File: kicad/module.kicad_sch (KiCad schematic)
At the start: 11 parts, among them J2 Conn_01x12, J3 Conn_01x10, J4 Conn_01x02, Q1 SI2302CDS, SW1 CNK_KMR2, U8 RioteeModule

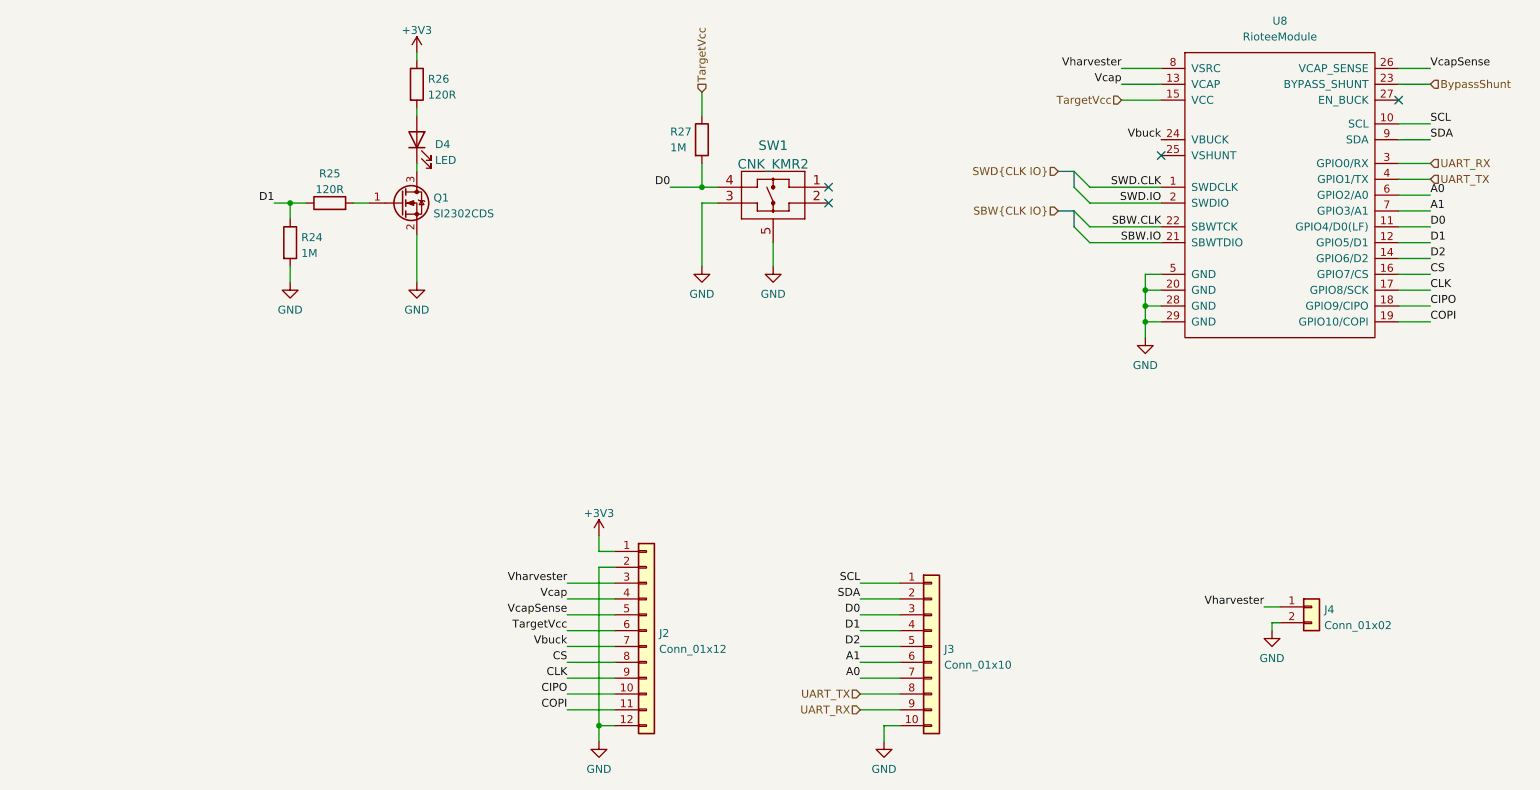
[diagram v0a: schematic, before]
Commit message: add fourth level converter for simultaneous programming + TX/RX
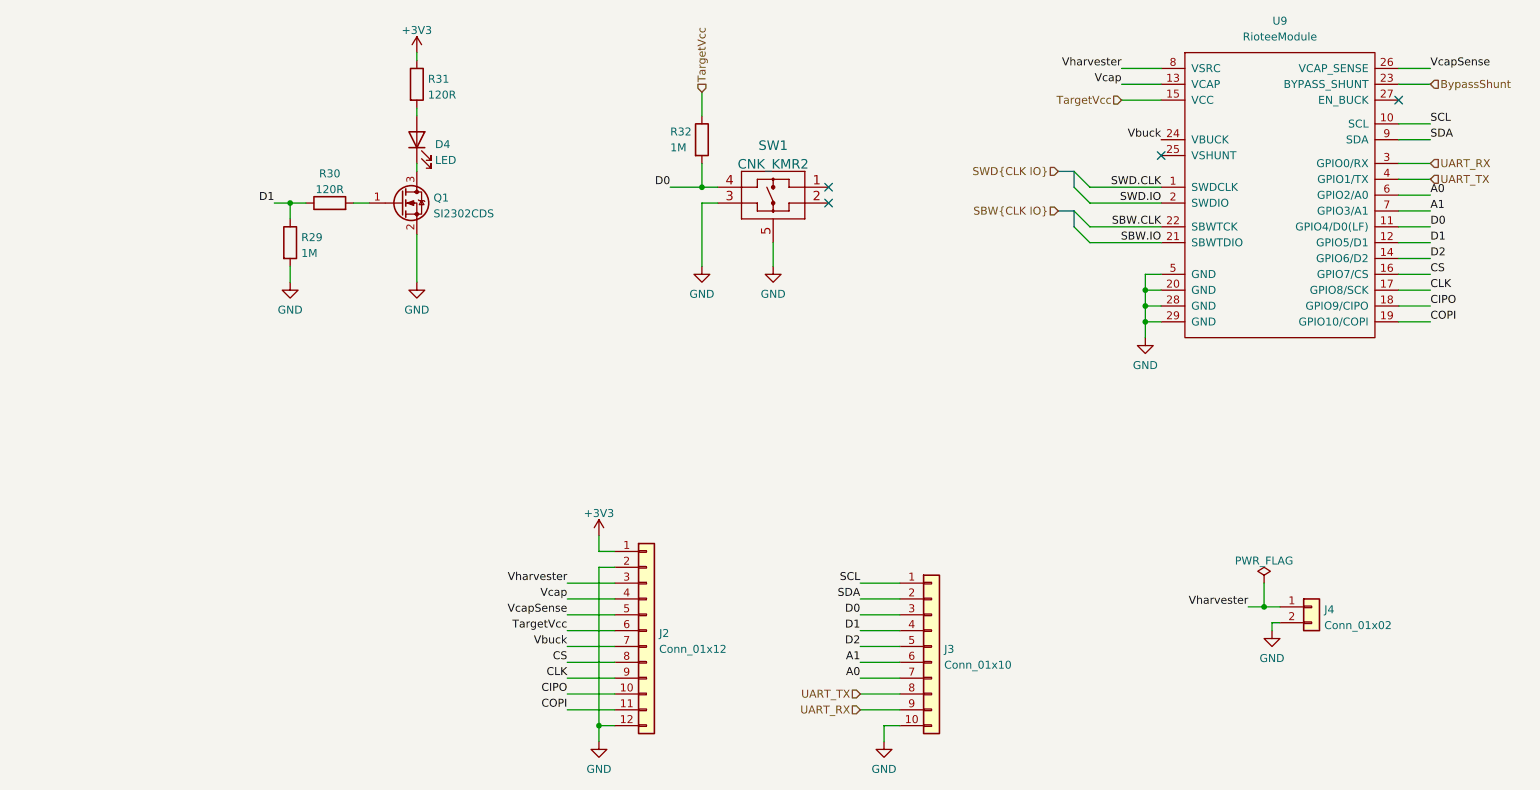
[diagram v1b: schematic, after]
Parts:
- renumbered R24 to R29, R25 to R30, R26 to R31, R27 to R32, U8 to U9

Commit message: replace target supply diode with analog switch
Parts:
- added C28: 0.1u, Capacitor_SMD:C_0402_1005Metric, symbol Device:C
- added R28: 5.1k, Resistor_SMD:R_0402_1005Metric, symbol Device:R
- added U9: TS5A3166YZP, riotee:TI_YZP0005, symbol riotee:TS5A3166YZP
- D3: renamed from D4; MPN (none) -> QBLP595-AG1
- J2: MPN (none) -> PPPC121LFBN-RC
- J3: MPN (none) -> PPPC101LFBN-RC
- J4: MPN (none) -> 620102131822
- Q1: MPN (none) -> SI2302CDS-T1-GE3
- R29, R32: MPN (none) -> WR04X1004FTL
- R30, R31: MPN (none) -> CR0402-FX-1200GLF
- SW1: MPN (none) -> KMR221NG LFS
- renumbered U9 to U10
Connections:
- net +3V3: now also C28.1, U9.A2 (V+)
- net GND: now also C28.2, R28.1, U9.C1 (GND)
- net TargetVcc: now also U9.A1
- new net +2V1: U9.B1
- new net TargetPowerEnable: R28.2, U9.C2

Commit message: rename pins and add component description
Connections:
- net GND: no longer SW1.5
- net CIPO renamed D9
- net CLK renamed D8
- net COPI renamed D10
- net CS renamed D7
- net D0 renamed D6
- net D1 renamed D5
- net D2 renamed D4
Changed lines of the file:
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@@
-    (stroke (width 0) (type default) (color 0 0 0 0))
-  )
-  (wire (pts (xy 135.89 60.96) (xy 135.89 64.77))
     (stroke (width 0) (type default) (color 0 0 0 0))
   )
@@
     (stroke (width 0) (type default) (color 0 0 0 0))
   )
-  (label "D1" (at 55.88 54.61 180)
+  (label "D5" (at 55.88 54.61 180)
     (effects (font (size 1.27 1.27)) (justify right bottom))
   )
@@
     (effects (font (size 1.27 1.27)) (justify right bottom))
   )
-  (label "COPI" (at 241.3 73.66 0)
+  (label "D10" (at 241.3 73.66 0)
     (effects (font (size 1.27 1.27)) (justify left bottom))
   )
@@
     (effects (font (size 1.27 1.27)) (justify right bottom))
   )
-  (label "D0" (at 119.38 52.07 180)
+  (label "D6" (at 119.38 52.07 180)
     (effects (font (size 1.27 1.27)) (justify right bottom))
   )
@@
     (effects (font (size 1.27 1.27)) (justify left bottom))
   )
-  (label "CS" (at 241.3 66.04 0)
+  (label "D7" (at 241.3 66.04 0)
     (effects (font (size 1.27 1.27)) (justify left bottom))
   )
@@
     (effects (font (size 1.27 1.27)) (justify right bottom))
   )
-  (label "COPI" (at 102.87 135.89 180)
+  (label "D10" (at 102.87 135.89 180)
     (effects (font (size 1.27 1.27)) (justify right bottom))
   )
@@
     (effects (font (size 1.27 1.27)) (justify right bottom))
   )
-  (label "CIPO" (at 102.87 133.35 180)
-    (effects (font (size 1.27 1.27)) (justify right bottom))
-  )
-  (label "D0" (at 149.86 120.65 180)
+  (label "D9" (at 102.87 133.35 180)
+    (effects (font (size 1.27 1.27)) (justify right bottom))
+  )
+  (label "D6" (at 149.86 120.65 180)
     (effects (font (size 1.27 1.27)) (justify right bottom))
   )
@@
     (effects (font (size 1.27 1.27)) (justify left bottom))
   )
-  (label "D2" (at 241.3 63.5 0)
-    (effects (font (size 1.27 1.27)) (justify left bottom))
-  )
-  (label "D0" (at 241.3 58.42 0)
+  (label "D4" (at 241.3 63.5 0)
+    (effects (font (size 1.27 1.27)) (justify left bottom))
+  )
+  (label "D6" (at 241.3 58.42 0)
     (effects (font (size 1.27 1.27)) (justify left bottom))
   )
@@
     (effects (font (size 1.27 1.27)) (justify right bottom))
   )
-  (label "D1" (at 241.3 60.96 0)
-    (effects (font (size 1.27 1.27)) (justify left bottom))
-  )
-  (label "D1" (at 149.86 123.19 180)
+  (label "D5" (at 241.3 60.96 0)
+    (effects (font (size 1.27 1.27)) (justify left bottom))
+  )
+  (label "D5" (at 149.86 123.19 180)
     (effects (font (size 1.27 1.27)) (justify right bottom))
   )
@@
     (effects (font (size 1.27 1.27)) (justify left bottom))
   )
-  (label "CIPO" (at 241.3 71.12 0)
+  (label "D9" (at 241.3 71.12 0)
     (effects (font (size 1.27 1.27)) (justify left bottom))
   )
@@
     (effects (font (size 1.27 1.27)) (justify right bottom))
   )
-  (label "CLK" (at 102.87 130.81 180)
-    (effects (font (size 1.27 1.27)) (justify right bottom))
-  )
-  (label "CLK" (at 241.3 68.58 0)
+  (label "D8" (at 102.87 130.81 180)
+    (effects (font (size 1.27 1.27)) (justify right bottom))
+  )
+  (label "D8" (at 241.3 68.58 0)
     (effects (font (size 1.27 1.27)) (justify left bottom))
   )
@@
     (effects (font (size 1.27 1.27)) (justify right bottom))
   )
-  (label "CS" (at 102.87 128.27 180)
-    (effects (font (size 1.27 1.27)) (justify right bottom))
-  )
-  (label "D2" (at 149.86 125.73 180)
+  (label "D7" (at 102.87 128.27 180)
+    (effects (font (size 1.27 1.27)) (justify right bottom))
+  )
+  (label "D4" (at 149.86 125.73 180)
     (effects (font (size 1.27 1.27)) (justify right bottom))
   )
@@
     )
     (property "MPN" "CR0402-FX-1200GLF" (id 4) (at 78.74 35.56 0)
+      (effects (font (size 1.27 1.27)) hide)
+    )
+    (property "Description" "Res, 0402, 1%" (id 5) (at 78.74 35.56 0)
       (effects (font (size 1.27 1.27)) hide)
     )
@@
       (effects (font (size 1.27 1.27)) hide)
     )
+    (property "Description" "Res, 0402, 1%" (id 5) (at 124.46 44.45 0)
+      (effects (font (size 1.27 1.27)) hide)
+    )
     (pin "1")
     (pin "2")
@@
       (effects (font (size 1.27 1.27)) hide)
     )
+    (property "Description" "Res, 0402, 1%" (id 5) (at 44.45 127 0)
+      (effects (font (size 1.27 1.27)) hide)
+    )
     (pin "1")
     (pin "2")
@@
     )
     (property "MPN" "CL05A104KA5NNNC" (id 4) (at 67.31 102.87 0)
+      (effects (font (size 1.27 1.27)) hide)
+    )
+    (property "Description" "Cap, 0402, X5R, 10V" (id 5) (at 67.31 102.87 0)
       (effects (font (size 1.27 1.27)) hide)
     )
@@
       (effects (font (size 1.27 1.27)) hide)
     )
+    (property "Description" "1-Ohm SPST switch" (id 5) (at 55.88 118.11 0)
+      (effects (font (size 1.27 1.27)) hide)
+    )
     (pin "A1")
     (pin "A2")
@@
       (effects (font (size 1.27 1.27)) hide)
     )
+    (property "Description" "Tactile SPST" (id 5) (at 135.89 53.34 0)
+      (effects (font (size 1.27 1.27)) hide)
+    )
     (pin "1")
     (pin "2")
     (pin "3")
     (pin "4")
-    (pin "5")
   )
   (symbol (lib_id "riotee:+2V1") (at 44.45 107.95 0) (unit 1)
@@
     )
     (property "MPN" "QBLP595-AG1" (id 4) (at 78.74 44.45 0)
+      (effects (font (size 1.27 1.27)) hide)
+    )
+    (property "Description" "LED, 0402, green, clear" (id 5) (at 78.74 44.45 0)
       (effects (font (size 1.27 1.27)) hide)
     )
@@
     )
     (property "MPN" "WR04X1004FTL" (id 4) (at 58.42 60.96 0)
+      (effects (font (size 1.27 1.27)) hide)
+    )
+    (property "Description" "Res, 0402, 1%" (id 5) (at 58.42 60.96 0)
       (effects (font (size 1.27 1.27)) hide)
     )
@@
     (pin "9")
   )
-  (symbol (lib_id "power:GND") (at 135.89 64.77 0) (unit 1)
-    (in_bom yes) (on_board yes) (fields_autoplaced)
-    (property "Reference" "#PWR061" (id 0) (at 135.89 71.12 0)
-      (effects (font (size 1.27 1.27)) hide)
-    )
-    (property "Value" "GND" (id 1) (at 135.89 69.2134 0))
-    (property "Footprint" "" (id 2) (at 135.89 64.77 0)
-      (effects (font (size 1.27 1.27)) hide)
-    )
-    (property "Datasheet" "" (id 3) (at 135.89 64.77 0)
-      (effects (font (size 1.27 1.27)) hide)
-    )
-    (pin "1")
-  )
   (symbol (lib_id "Device:R") (at 64.77 54.61 90) (unit 1)
     (in_bom yes) (on_board yes) (fields_autoplaced)
@@
       (effects (font (size 1.27 1.27)) hide)
     )
+    (property "Description" "Res, 0402, 1%" (id 5) (at 64.77 54.61 0)
+      (effects (font (size 1.27 1.27)) hide)
+    )
     (pin "1")
     (pin "2")
@@
       (effects (font (size 1.27 1.27)) hide)
     )
+    (property "Description" "MOSFET, N-Channel, Vth=0.6V" (id 5) (at 76.2 54.61 0)
+      (effects (font (size 1.27 1.27)) hide)
+    )

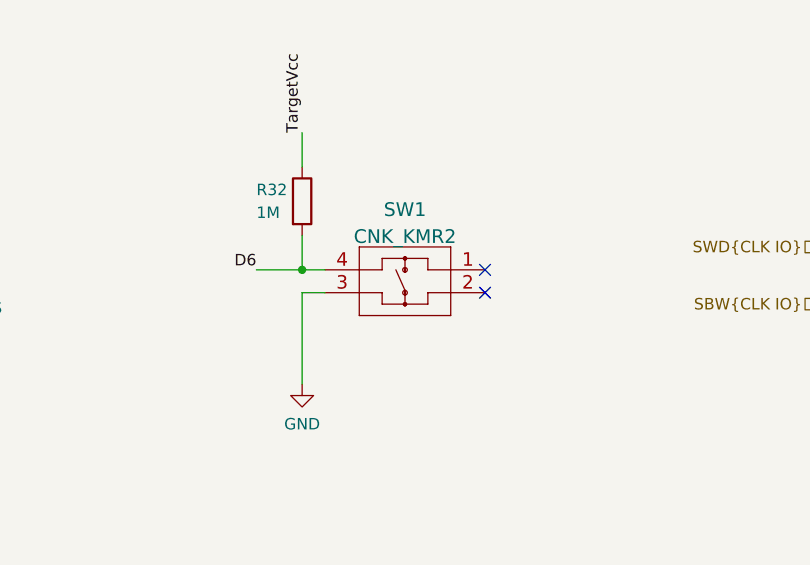
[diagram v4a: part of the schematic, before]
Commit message: migrate project to kicad 7
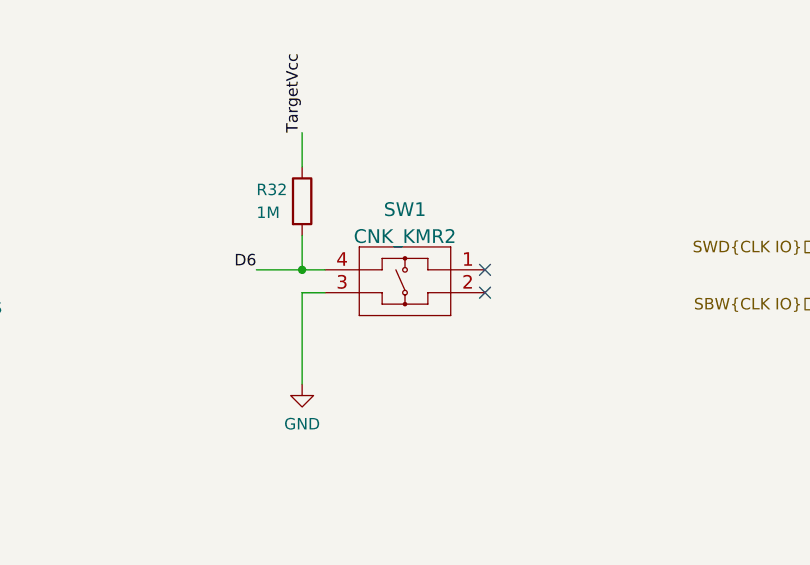
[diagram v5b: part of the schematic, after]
